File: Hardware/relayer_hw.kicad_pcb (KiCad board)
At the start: 4 copper layers, 41 x 88.5 mm, 58 parts, among them J2 AC_OUT, J4 AC_IN, Q1 2N7002, SW1 NRST, SW2 USR_SW, U1 STM32WB55, U2 902-9040, U3 LM1117-3.3, Y1 Crystal, Y2 Crystal_GND23

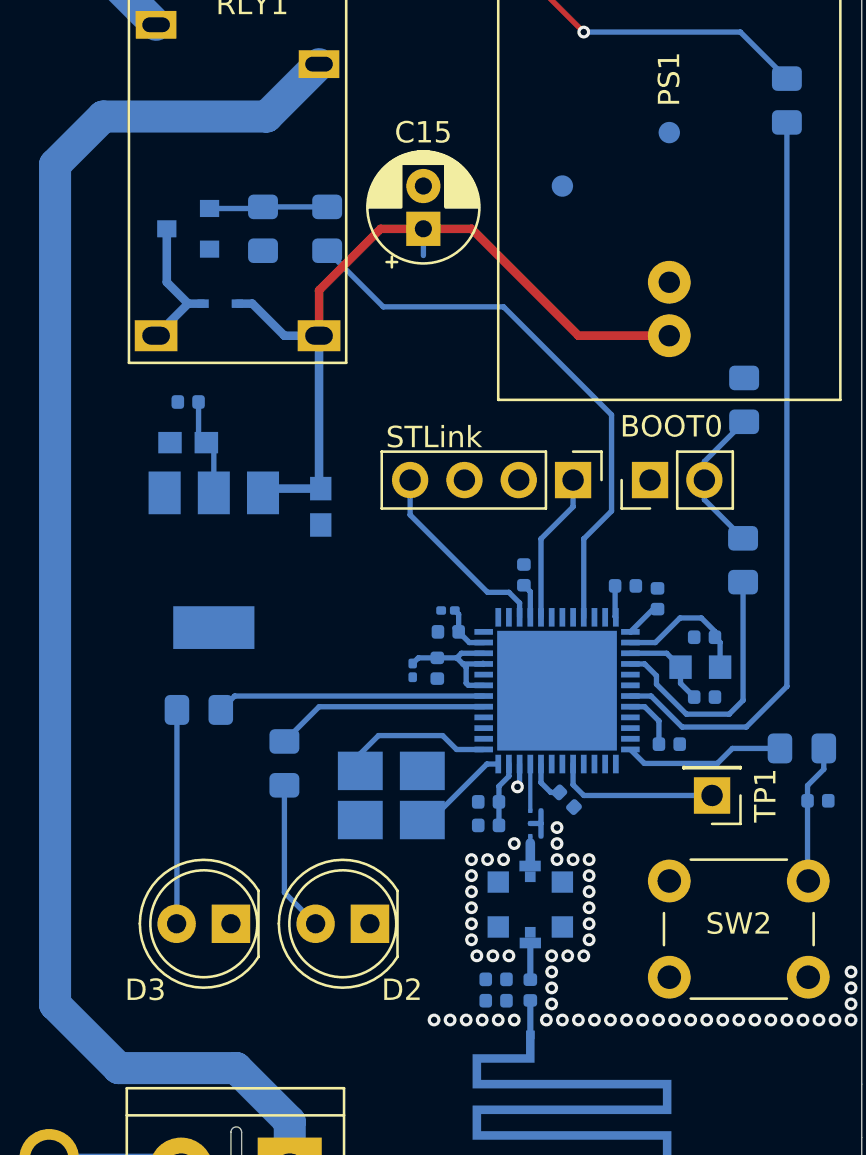
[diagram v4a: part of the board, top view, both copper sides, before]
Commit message: RF via fences
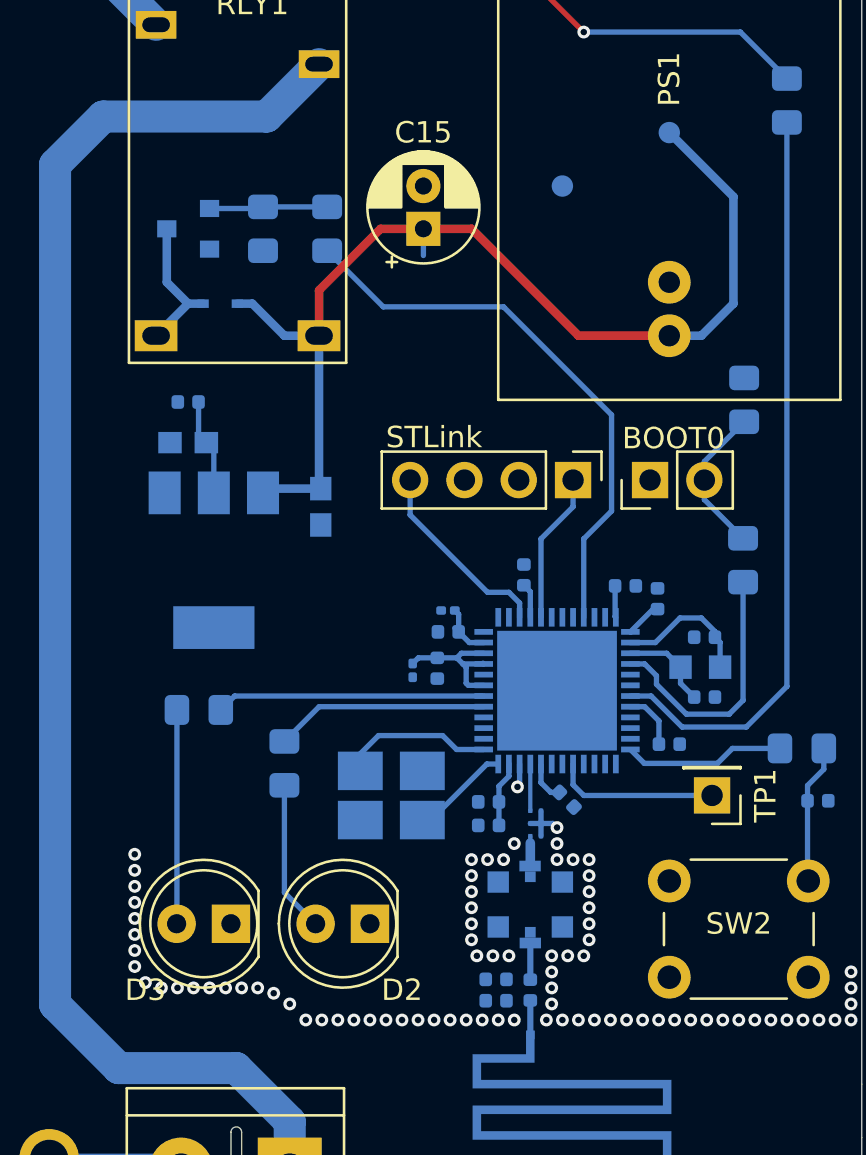
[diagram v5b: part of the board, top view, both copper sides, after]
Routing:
- net 5V: track 37.4 -> 50.3 mm
- net GND: track 6.87 -> 7.70 mm, vias 58 -> 84
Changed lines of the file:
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@@
     (thickness 1.6)
     (drawings 21)
-    (tracks 245)
+    (tracks 277)
     (zones 0)
     (modules 58)
@@
     (solder_mask_min_width 0.25)
     (aux_axis_origin 0 0)
-    (visible_elements 7FFFF7FF)
+    (visible_elements 7FFFFFFF)
     (pcbplotparams
       (layerselection 0x010fc_ffffffff)
@@
     (descr "Through hole straight pin header, 1x02, 2.54mm pitch, single row")
     (tags "Through hole pin header THT 1x02 2.54mm single row")
-    (fp_text reference BOOT0 (at 2.5 1) (layer F.SilkS)
+    (fp_text reference BOOT0 (at 1.95 1.1) (layer F.SilkS)
       (effects (font (size 1 1) (thickness 0.15)))
     )
@@
   (segment (start 144.2 105.15) (end 144 105.35) (width 0.4) (layer B.Cu) (net 7))
   (segment (start 146.7 105.15) (end 144.2 105.15) (width 0.4) (layer B.Cu) (net 7))
+  (segment (start 163 98) (end 164.5 98) (width 0.4) (layer B.Cu) (net 7))
+  (segment (start 164.5 98) (end 166 96.5) (width 0.4) (layer B.Cu) (net 7))
+  (segment (start 166 91.5) (end 163 88.5) (width 0.4) (layer B.Cu) (net 7))
+  (segment (start 166 96.5) (end 166 91.5) (width 0.4) (layer B.Cu) (net 7))
   (segment (start 140.5 96.5) (end 139 98) (width 0.4) (layer B.Cu) (net 8))
   (segment (start 141.2 96.5) (end 140.5 96.5) (width 0.4) (layer B.Cu) (net 8))
@@
   (segment (start 157 121.4) (end 157 120.81) (width 0.25) (layer B.Cu) (net 50))
   (segment (start 156.5 120.81) (end 157 120.81) (width 0.25) (layer B.Cu) (net 50))
+  (via (at 151.25 130) (size 0.6) (drill 0.3) (layers F.Cu B.Cu) (net 50))
+  (via (at 150.5 130) (size 0.6) (drill 0.3) (layers F.Cu B.Cu) (net 50))
+  (via (at 149.75 130) (size 0.6) (drill 0.3) (layers F.Cu B.Cu) (net 50))
+  (via (at 149 130) (size 0.6) (drill 0.3) (layers F.Cu B.Cu) (net 50))
+  (via (at 148.25 130) (size 0.6) (drill 0.3) (layers F.Cu B.Cu) (net 50))
+  (via (at 147.5 130) (size 0.6) (drill 0.3) (layers F.Cu B.Cu) (net 50))
+  (via (at 146.75 130) (size 0.6) (drill 0.3) (layers F.Cu B.Cu) (net 50))
+  (via (at 146 130) (size 0.6) (drill 0.3) (layers F.Cu B.Cu) (net 50))
+  (via (at 145.25 129.25) (size 0.6) (drill 0.3) (layers F.Cu B.Cu) (net 50))
+  (via (at 144.5 128.75) (size 0.6) (drill 0.3) (layers F.Cu B.Cu) (net 50))
+  (via (at 143.75 128.5) (size 0.6) (drill 0.3) (layers F.Cu B.Cu) (net 50))
+  (via (at 143 128.5) (size 0.6) (drill 0.3) (layers F.Cu B.Cu) (net 50))
+  (via (at 142.25 128.5) (size 0.6) (drill 0.3) (layers F.Cu B.Cu) (net 50))
+  (via (at 141.5 128.5) (size 0.6) (drill 0.3) (layers F.Cu B.Cu) (net 50))
+  (via (at 140.75 128.5) (size 0.6) (drill 0.3) (layers F.Cu B.Cu) (net 50))
+  (via (at 140 128.5) (size 0.6) (drill 0.3) (layers F.Cu B.Cu) (net 50))
+  (via (at 139.25 128.5) (size 0.6) (drill 0.3) (layers F.Cu B.Cu) (net 50))
+  (via (at 138.5 128.25) (size 0.6) (drill 0.3) (layers F.Cu B.Cu) (net 50))
+  (via (at 138 127.5) (size 0.6) (drill 0.3) (layers F.Cu B.Cu) (net 50))
+  (via (at 138 126.75) (size 0.6) (drill 0.3) (layers F.Cu B.Cu) (net 50))
+  (via (at 138 126) (size 0.6) (drill 0.3) (layers F.Cu B.Cu) (net 50))
+  (via (at 138 125.25) (size 0.6) (drill 0.3) (layers F.Cu B.Cu) (net 50))
+  (via (at 138 124.5) (size 0.6) (drill 0.3) (layers F.Cu B.Cu) (net 50))
+  (via (at 138 123.75) (size 0.6) (drill 0.3) (layers F.Cu B.Cu) (net 50))
+  (via (at 138 123) (size 0.6) (drill 0.3) (layers F.Cu B.Cu) (net 50))
+  (via (at 138 122.25) (size 0.6) (drill 0.3) (layers F.Cu B.Cu) (net 50))
+  (segment (start 157.56 120.81) (end 157.75 121) (width 0.25) (layer B.Cu) (net 50))
+  (segment (start 157 120.81) (end 157.56 120.81) (width 0.25) (layer B.Cu) (net 50))
   (segment (start 146.33 60.17) (end 134.27501 72.22499) (width 1.5) (layer B.Cu) (net 51))
   (segment (start 146.33 57.5) (end 146.33 60.17) (width 1.5) (layer B.Cu) (net 51))

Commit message: Conectando nos n conectados / planos de terra e vcc
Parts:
- moved C5 0.20 mm to (152.4, 110.8)
- moved C6 0.20 mm to (152.5, 111.8)
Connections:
- U1 pad 49: (no net) -> GND
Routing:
- net Net-(J2-Pad1): track 69.1 -> 138.1 mm
- net N: track 62.8 -> 76.0 mm
- net 3V3: track 26.5 -> 28.5 mm, vias 0 -> 16
- net 5V: track 50.3 -> 49.0 mm
- net Net-(U2-Pad2): track 1.72 -> 2.84 mm
- net Net-(Z2-Pad1): track 1.61 -> 2.74 mm
- net GND: track 7.70 -> 8.70 mm, vias 84 -> 86
- added copper zone on VCC, net 3V3
- added copper zone on B.Cu, net GND
- added copper zone on F.Cu, net GND
- added copper zone on GND, net GND
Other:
- outline, holes or cut-outs redrawn

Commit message: Correçoes de pepinos do DRC
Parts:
- renumbered BOOT0 to J1, STLink to J3, N to JP1
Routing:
- net 3V3: track 28.5 -> 26.8 mm
- net GND: track 8.70 -> 9.11 mm, vias 86 -> 103
- net Net-(J2-Pad1): vias 0 -> 28
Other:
- rule pad_to_mask_clearance: 0.051 -> 0.127

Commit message: Versao final dos planos de gnd e vcc (?)
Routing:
- net GND: track 9.11 -> 11.4 mm, vias 103 -> 109
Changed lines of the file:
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@@
     (thickness 1.6)
     (drawings 29)
-    (tracks 395)
+    (tracks 403)
     (zones 0)
     (modules 58)
@@
   (page A4)
   (layers
-    (0 F.Cu signal)
+    (0 F.Cu signal hide)
     (1 VCC power hide)
     (2 GND power hide)
@@
   (gr_line (start 172 53.5) (end 172 133) (layer Edge.Cuts) (width 0.05))
   (gr_line (start 132.5 53) (end 171.5 53) (layer Edge.Cuts) (width 0.05))
+  (segment (start 147.25 121.75) (end 146 121.75) (width 0.25) (layer GND) (net 50))
   (segment (start 165.375 112.34) (end 165.375 113.5) (width 0.25) (layer B.Cu) (net 1))
   (segment (start 165.135 112.1) (end 165.375 112.34) (width 0.25) (layer B.Cu) (net 1))
@@
   (segment (start 156.485 129.1) (end 156.5 129.085) (width 0.25) (layer B.Cu) (net 49))
   (segment (start 155.385 129.1) (end 156.485 129.1) (width 0.25) (layer B.Cu) (net 49))
-  (via (at 151.5 118.5) (size 0.6) (drill 0.3) (layers F.Cu B.Cu) (net 50))
+  (via (at 152 118.75) (size 0.6) (drill 0.3) (layers F.Cu B.Cu) (net 50))
+  (via (at 151 118.75) (size 0.6) (drill 0.3) (layers F.Cu B.Cu) (net 50))
+  (via (at 152 118) (size 0.6) (drill 0.3) (layers F.Cu B.Cu) (net 50))
+  (via (at 151 118) (size 0.6) (drill 0.3) (layers F.Cu B.Cu) (net 50))
+  (via (at 148 121) (size 0.6) (drill 0.3) (layers F.Cu B.Cu) (net 50))
+  (via (at 149 121) (size 0.6) (drill 0.3) (layers F.Cu B.Cu) (net 50))
+  (via (at 149 120.25) (size 0.6) (drill 0.3) (layers F.Cu B.Cu) (net 50))
+  (via (at 148 120.25) (size 0.6) (drill 0.3) (layers F.Cu B.Cu) (net 50))
   (via (at 155.5 114) (size 0.6) (drill 0.3) (layers F.Cu B.Cu) (net 50))
   (via (at 160 117) (size 0.6) (drill 0.3) (layers F.Cu B.Cu) (net 50))
   (via (at 158.5 117) (size 0.6) (drill 0.3) (layers F.Cu B.Cu) (net 50))
   (via (at 157 117) (size 0.6) (drill 0.3) (layers F.Cu B.Cu) (net 50))
-  (via (at 155.5 117) (size 0.6) (drill 0.3) (layers F.Cu B.Cu) (net 50))
   (via (at 155.5 115.5) (size 0.6) (drill 0.3) (layers F.Cu B.Cu) (net 50))
   (via (at 157 115.5) (size 0.6) (drill 0.3) (layers F.Cu B.Cu) (net 50))
@@
   (segment (start 155.35 113.85) (end 155.5 114) (width 0.25) (layer B.Cu) (net 50))
   (segment (start 154.32 113.85) (end 155.35 113.85) (width 0.25) (layer B.Cu) (net 50))
+  (segment (start 165.1 114.9) (end 165.1 115.9) (width 0.25) (layer GND) (net 50))
   (segment (start 146.33 60.17) (end 134.27501 72.22499) (width 1.5) (layer B.Cu) (net 51))
   (segment (start 146.33 57.5) (end 146.33 60.17) (width 1.5) (layer B.Cu) (net 51))
@@
     )
   )
-  (zone (net 50) (net_name GND) (layer F.Cu) (hatch edge 0.508)
+  (zone (net 0) (net_name "") (layer B.Mask) (hatch edge 0.508)
     (connect_pads (clearance 0.2))
     (min_thickness 0.254)
@@
     (polygon
       (pts
-        (xy 172 130.5) (xy 137.5 130.5) (xy 137.5 61.499647) (xy 148.5 61.5) (xy 148.5 53)
-        (xy 172 53)
+        (xy 138.9 137.8) (xy 135.2 137.8) (xy 135.2 136.2) (xy 138.9 136.2)
       )
     )
   )
-  (zone (net 0) (net_name "") (layer B.Mask) (hatch edge 0.508)
+  (zone (net 50) (net_name GND) (layer B.Cu) (hatch edge 0.508)
     (connect_pads (clearance 0.2))
     (min_thickness 0.254)
@@
     (polygon
       (pts
-        (xy 138.9 137.8) (xy 135.2 137.8) (xy 135.2 136.2) (xy 138.9 136.2)
+        (xy 148.5 61.5) (xy 148.5 53) (xy 172 53) (xy 172 115.75) (xy 166.75 115.75)
+        (xy 166.75 111) (xy 162 111) (xy 162 112.25) (xy 160.75 112.25) (xy 160.75 113.25)
+        (xy 161.75 113.25) (xy 161.75 115.75) (xy 166.75 115.75) (xy 172 115.75) (xy 172 130.5)
+        (xy 137.5 130.5) (xy 137.5 61.5)
+      )
+    )
+    (polygon
+      (pts
+        (xy 153.25 122.25) (xy 153.25 119) (xy 155.25 119) (xy 155.25 117) (xy 153.5 117)
+        (xy 153.5 116.75) (xy 146.75 116.75) (xy 146.75 122.25)
+      )
+    )
+  )
+  (zone (net 50) (net_name GND) (layer F.Cu) (hatch edge 0.508)
+    (connect_pads (clearance 0.2))
+    (min_thickness 0.254)
+    (fill yes (arc_segments 32) (thermal_gap 0.508) (thermal_bridge_width 0.508))
+    (polygon
+      (pts
+        (xy 148.5 61.5) (xy 148.5 53) (xy 172 53) (xy 172 115.75) (xy 166.75 115.75)
+        (xy 166.75 111) (xy 162 111) (xy 162 112.25) (xy 160.75 112.25) (xy 160.75 113.25)
+        (xy 161.75 113.25) (xy 161.75 115.75) (xy 166.75 115.75) (xy 172 115.75) (xy 172 130.5)
+        (xy 137.5 130.5) (xy 137.5 61.5)
+      )
+    )
+    (polygon
+      (pts
+        (xy 153.25 122.25) (xy 153.25 119) (xy 155.25 119) (xy 155.25 117) (xy 153.5 117)
+        (xy 153.5 116.75) (xy 146.75 116.75) (xy 146.75 122.25)
       )
     )
@@
     (polygon
       (pts
-        (xy 172 130.5) (xy 137.5 130.5) (xy 137.5 53) (xy 172 53)
+        (xy 137.5 53) (xy 148.5 53) (xy 172 53) (xy 172 115.75) (xy 166.75 115.75)
+        (xy 166.75 111) (xy 162 111) (xy 162 112.25) (xy 160.75 112.25) (xy 160.75 113.25)
+        (xy 161.75 113.25) (xy 161.75 115.75) (xy 166.75 115.75) (xy 172 115.75) (xy 172 130.5)
+        (xy 137.5 130.5) (xy 137.5 61.5)
+      )
+    )
+    (polygon
+      (pts
+        (xy 153.25 122.25) (xy 153.25 119) (xy 155.25 119) (xy 155.25 117) (xy 153.5 117)
+        (xy 153.5 116.75) (xy 146.75 116.75) (xy 146.75 122.25)
       )
     )
@@
     (polygon
       (pts
-        (xy 172 130.5) (xy 137.5 130.5) (xy 137.5 53) (xy 172 53)
+        (xy 137.5 53) (xy 148.5 53) (xy 172 53) (xy 172 115.75) (xy 166.75 115.75)
+        (xy 166.75 111) (xy 161.75 111) (xy 161.75 112) (xy 160.5 112) (xy 160.5 113.5)
+        (xy 161.75 113.5) (xy 161.75 115.75) (xy 166.75 115.75) (xy 172 115.75) (xy 172 130.5)
+        (xy 137.5 130.5) (xy 137.5 61.5)
+      )
+    )
+    (polygon
+      (pts
+        (xy 153.25 122.25) (xy 153.25 119) (xy 155.5 119) (xy 155.5 116.75) (xy 153.5 116.75)
+        (xy 146.75 116.75) (xy 146.75 122.25)
       )
     )
   )
-  (zone (net 50) (net_name GND) (layer B.Cu) (hatch edge 0.508)
+  (zone (net 50) (net_name GND) (layer GND) (hatch edge 0.508)
+    (connect_pads (clearance 0.2))
+    (min_thickness 0.254)
+    (fill yes (arc_segments 32) (thermal_gap 0.508) (thermal_bridge_width 0.508))
+    (polygon
+      (pts
+        (xy 155.25 118.75) (xy 153 118.75) (xy 153 122) (xy 147 122) (xy 147 117)
+        (xy 155.25 117)
+      )
+    )
+  )
+  (zone (net 50) (net_name GND) (layer GND) (hatch edge 0.508)
     (connect_pads (clearance 0.2))
     (min_thickness 0.254)
@@
     (polygon
       (pts
-        (xy 172 130.5) (xy 137.5 130.5) (xy 137.5 61.5) (xy 148.5 61.5) (xy 148.5 53)
-        (xy 172 53)
+        (xy 166.5 115.5) (xy 162 115.5) (xy 162 113) (xy 160.75 113) (xy 160.75 112.25)
+        (xy 162 112.25) (xy 162 111.25) (xy 166.5 111.25)
       )
     )
